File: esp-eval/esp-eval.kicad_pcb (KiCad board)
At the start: 2 copper layers, 26 parts, among them J1 ESP-ADAPT-1, J10 ESP-ADAPT-2-SHIELD, J2 ESP-ADAPT-2, J3 ESP-ADAPT-1-DBG, J4 ESP-ADAPT-2-DBG, J5 GPIO0-SEL, J6 GPIO2-SEL, J7 GPIO15-SEL, J8 USB-FTDI, J9 ESP-ADAPT-1-SHIELD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

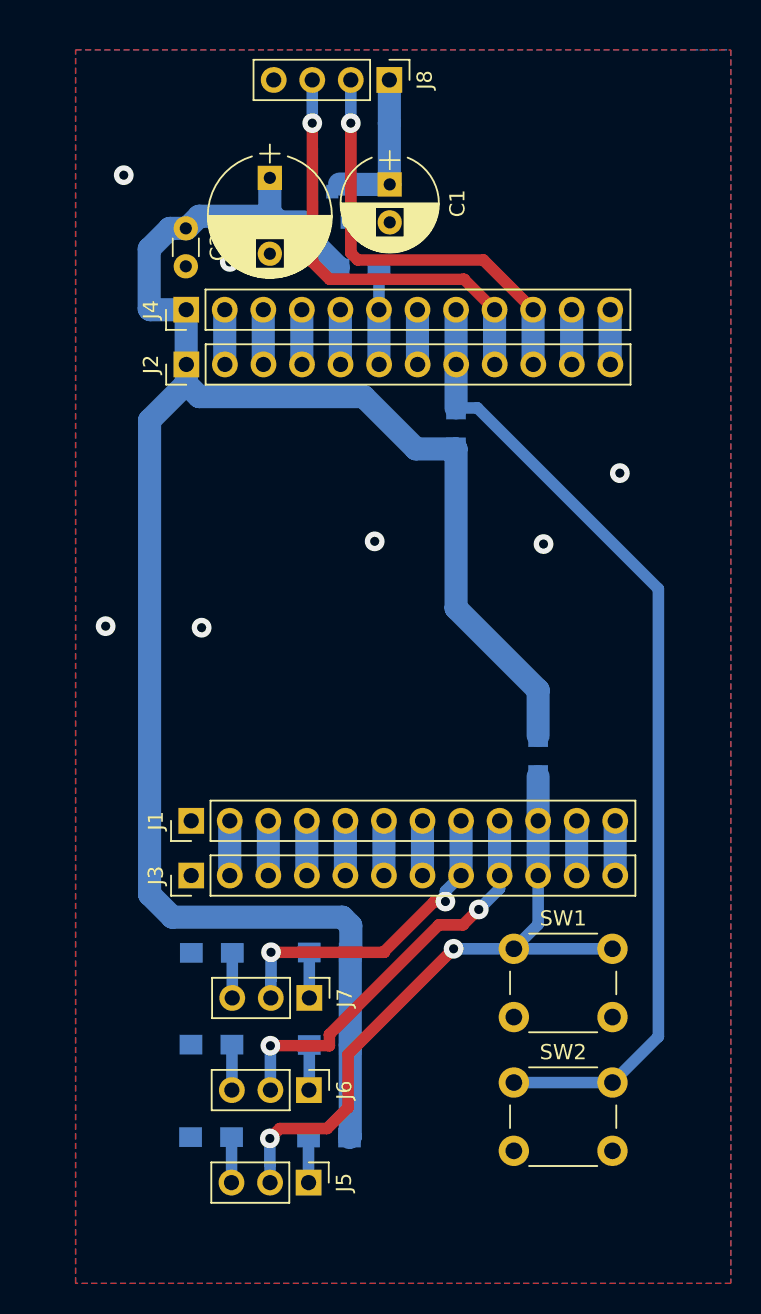
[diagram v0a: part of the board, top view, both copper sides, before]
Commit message: otwory montazowe
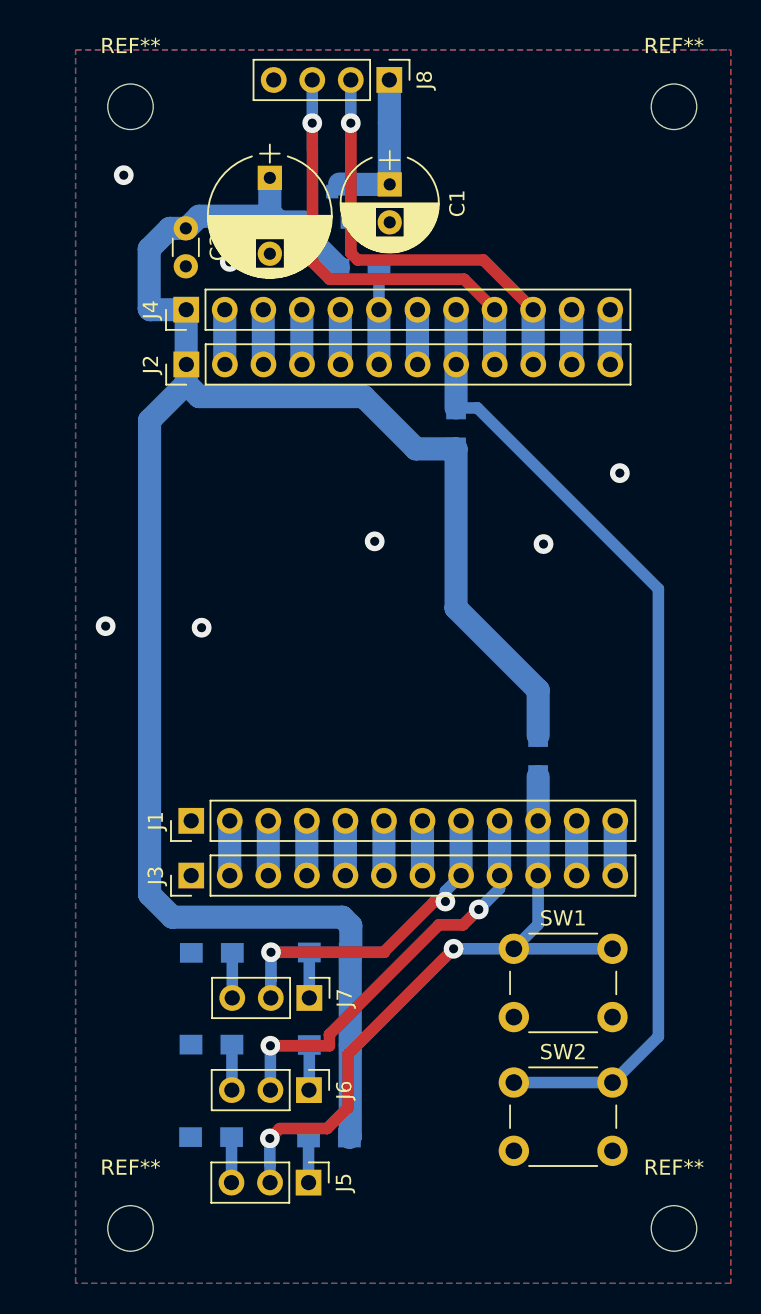
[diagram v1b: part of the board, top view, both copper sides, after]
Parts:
- added REF**: MountingHole_3mm, Mounting_Holes:MountingHole_3mm, F.Cu at (114.7, 23.5)
- added REF**: MountingHole_3mm, Mounting_Holes:MountingHole_3mm, F.Cu at (78.9, 23.5)
- added REF**: MountingHole_3mm, Mounting_Holes:MountingHole_3mm, F.Cu at (114.7, 97.4)
- added REF**: MountingHole_3mm, Mounting_Holes:MountingHole_3mm, F.Cu at (78.9, 97.4)
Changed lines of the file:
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@@
     (tracks 287)
     (zones 0)
-    (modules 26)
+    (modules 30)
     (nets 53)
   )
@@
     (add_net GND)
     (add_net VBUS)
+  )
+  (module Mounting_Holes:MountingHole_3mm (layer F.Cu)
+    (at 114.681 23.495)
+    (descr "Mounting Hole 3mm, no annular")
+    (tags "mounting hole 3mm no annular")
+    (attr virtual)
+    (fp_text reference REF** (at 0 -4) (layer F.SilkS)
+      (effects (font (size 1 1) (thickness 0.15)))
+    )
+    (fp_text value MountingHole_3mm (at 0 4) (layer F.Fab)
+      (effects (font (size 1 1) (thickness 0.15)))
+    )
+    (fp_circle (center 0 0) (end 3.25 0) (layer F.CrtYd) (width 0.05))
+    (fp_circle (center 0 0) (end 3 0) (layer Cmts.User) (width 0.15))
+    (fp_text user %R (at 0.3 0) (layer F.Fab)
+      (effects (font (size 1 1) (thickness 0.15)))
+    )
+    (pad 1 np_thru_hole circle (at 0 0) (size 3 3) (drill 3) (layers *.Cu *.Mask))
+  )
+  (module Mounting_Holes:MountingHole_3mm (layer F.Cu)
+    (at 78.867 23.495)
+    (descr "Mounting Hole 3mm, no annular")
+    (tags "mounting hole 3mm no annular")
+    (attr virtual)
+    (fp_text reference REF** (at 0 -4) (layer F.SilkS)
+      (effects (font (size 1 1) (thickness 0.15)))
+    )
+    (fp_text value MountingHole_3mm (at 0 4) (layer F.Fab)
+      (effects (font (size 1 1) (thickness 0.15)))
+    )
+    (fp_circle (center 0 0) (end 3.25 0) (layer F.CrtYd) (width 0.05))
+    (fp_circle (center 0 0) (end 3 0) (layer Cmts.User) (width 0.15))
+    (fp_text user %R (at 0.3 0) (layer F.Fab)
+      (effects (font (size 1 1) (thickness 0.15)))
+    )
+    (pad 1 np_thru_hole circle (at 0 0) (size 3 3) (drill 3) (layers *.Cu *.Mask))
+  )
+  (module Mounting_Holes:MountingHole_3mm (layer F.Cu)
+    (at 114.681 97.409)
+    (descr "Mounting Hole 3mm, no annular")
+    (tags "mounting hole 3mm no annular")
+    (attr virtual)
+    (fp_text reference REF** (at 0 -4) (layer F.SilkS)
+      (effects (font (size 1 1) (thickness 0.15)))
+    )
+    (fp_text value MountingHole_3mm (at 0 4) (layer F.Fab)
+      (effects (font (size 1 1) (thickness 0.15)))
+    )
+    (fp_circle (center 0 0) (end 3.25 0) (layer F.CrtYd) (width 0.05))
+    (fp_circle (center 0 0) (end 3 0) (layer Cmts.User) (width 0.15))
+    (fp_text user %R (at 0.3 0) (layer F.Fab)
+      (effects (font (size 1 1) (thickness 0.15)))
+    )
+    (pad 1 np_thru_hole circle (at 0 0) (size 3 3) (drill 3) (layers *.Cu *.Mask))
   )
   (module Capacitors_ThroughHole:C_Disc_D3.0mm_W1.6mm_P2.50mm (layer F.Cu)
@@
     )
   )
+  (module Mounting_Holes:MountingHole_3mm (layer F.Cu)
+    (at 78.867 97.409)
+    (descr "Mounting Hole 3mm, no annular")
+    (tags "mounting hole 3mm no annular")
+    (attr virtual)
+    (fp_text reference REF** (at 0 -4) (layer F.SilkS)
+      (effects (font (size 1 1) (thickness 0.15)))
+    )
+    (fp_text value MountingHole_3mm (at 0 4) (layer F.Fab)
+      (effects (font (size 1 1) (thickness 0.15)))
+    )
+    (fp_text user %R (at 0.3 0) (layer F.Fab)
+      (effects (font (size 1 1) (thickness 0.15)))
+    )
+    (fp_circle (center 0 0) (end 3 0) (layer Cmts.User) (width 0.15))
+    (fp_circle (center 0 0) (end 3.25 0) (layer F.CrtYd) (width 0.05))
+    (pad 1 np_thru_hole circle (at 0 0) (size 3 3) (drill 3) (layers *.Cu *.Mask))
+  )
   (via (at 106.0831 52.3113) (size 1.3) (drill 0.6) (layers F.Cu B.Cu) (net 1))

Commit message: ulozenie plytek
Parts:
- moved U2 19.3 mm to (53.6, 51.5)
- moved J9 19.3 mm to (25.6, 70.9)
- moved J10 19.3 mm to (25.3, 40.8)

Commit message: napisy
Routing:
- net /RXD0: track 28.9 -> 29.4 mm, vias 1 -> 2
- net /TXD0: track 28.6 -> 29.0 mm, vias 1 -> 2
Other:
- board text added: "0"
- board text added: "1"
- board text added: "5V"
- board text added: "GND"
- board text added: "GPIO0"
- board text added: "GPIO15"
- board text added: "GPIO2"
- board text added: "RST"
- board text added: "RXD0"
- board text added: "TXD0"
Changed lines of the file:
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@@
   (general
     (thickness 1.6)
-    (drawings 4)
-    (tracks 287)
+    (drawings 15)
+    (tracks 298)
     (zones 0)
     (modules 30)
@@
   (layers
     (0 F.Cu signal)
-    (31 B.Cu signal)
+    (31 B.Cu signal hide)
     (32 B.Adhes user)
     (33 F.Adhes user hide)
@@
     (pad 1 np_thru_hole circle (at 0 0) (size 3 3) (drill 3) (layers *.Cu *.Mask))
   )
+  (gr_text RST (at 116.84 89.9922 90) (layer F.Cu)
+    (effects (font (size 1.5 1.5) (thickness 0.3)))
+  )
+  (gr_text GPIO0 (at 116.7892 81.3308 90) (layer F.Cu)
+    (effects (font (size 1.5 1.5) (thickness 0.3)))
+  )
+  (gr_text 1 (at 90.5764 96.7232) (layer F.Cu)
+    (effects (font (size 1.5 1.5) (thickness 0.3)))
+  )
+  (gr_text 0 (at 85.4964 96.774) (layer F.Cu)
+    (effects (font (size 1.5 1.5) (thickness 0.3)))
+  )
+  (gr_text GPIO0 (at 82.8548 91.3384) (layer F.Cu)
+    (effects (font (size 1.5 1.5) (thickness 0.3)))
+  )
+  (gr_text GPIO2 (at 82.8802 85.2932) (layer F.Cu)
+    (effects (font (size 1.5 1.5) (thickness 0.3)))
+  )
+  (gr_text GPIO15 (at 82.2198 79.0956) (layer F.Cu)
+    (effects (font (size 1.5 1.5) (thickness 0.3)))
+  )
+  (gr_text 5V (at 107.5436 21.9964 90) (layer F.Cu)
+    (effects (font (size 1.5 1.5) (thickness 0.3)))
+  )
+  (gr_text TXD0 (at 105.0036 23.1648 90) (layer F.Cu)
+    (effects (font (size 1.5 1.5) (thickness 0.3)))
+  )
+  (gr_text RXD0 (at 102.4636 23.2918 90) (layer F.Cu)
+    (effects (font (size 1.5 1.5) (thickness 0.3)))
+  )
+  (gr_text GND (at 99.8982 22.6314 90) (layer F.Cu)
+    (effects (font (size 1.5 1.5) (thickness 0.3)))
+  )
   (dimension 81.127636 (width 0.3) (layer F.SilkS)
     (gr_text "81,128 mm" (at 126.825905 60.383783 89.94618432) (layer F.SilkS)
@@
   (via (at 90.8431 24.5745) (size 1.3) (drill 0.6) (layers F.Cu B.Cu) (net 17))
   (segment (start 90.8431 24.5745) (end 90.8431 21.7297) (width 0.762) (layer B.Cu) (net 17) (status 20))
-  (segment (start 100.8505 34.8615) (end 102.8575 36.8685) (width 0.762) (layer F.Cu) (net 17) (status 20))
-  (segment (start 91.9861 34.8615) (end 100.8505 34.8615) (width 0.762) (layer F.Cu) (net 17))
-  (segment (start 90.8685 33.7439) (end 91.9861 34.8615) (width 0.762) (layer F.Cu) (net 17))
-  (segment (start 90.8431 24.5745) (end 90.8685 33.7439) (width 0.762) (layer F.Cu) (net 17))
+  (segment (start 90.8431 24.5745) (end 90.8558 32.9692) (width 0.762) (layer F.Cu) (net 17))
+  (segment (start 90.8558 32.9692) (end 90.8558 33.02) (width 0.762) (layer F.Cu) (net 17))
+  (via (at 101.3714 34.3916) (size 1.3) (drill 0.6) (layers F.Cu B.Cu) (net 17))
+  (segment (start 90.8558 33.02) (end 92.2274 34.3916) (width 0.762) (layer F.Cu) (net 17))
+  (segment (start 92.2274 34.3916) (end 101.3714 34.3916) (width 0.762) (layer F.Cu) (net 17))
+  (segment (start 101.3714 34.3916) (end 101.9302 34.3916) (width 0.762) (layer B.Cu) (net 17))
+  (segment (start 102.8575 35.3189) (end 102.8575 36.8685) (width 0.762) (layer B.Cu) (net 17))
+  (segment (start 101.9302 34.3916) (end 102.8575 35.3189) (width 0.762) (layer B.Cu) (net 17))
   (segment (start 105.3975 40.464898) (end 105.407502 40.4749) (width 1.524) (layer B.Cu) (net 18) (status 30))
   (segment (start 105.3975 36.8685) (end 105.3975 40.464898) (width 1.524) (layer B.Cu) (net 18) (status 30))
   (via (at 93.3831 24.5745) (size 1.3) (drill 0.6) (layers F.Cu B.Cu) (net 18))
   (segment (start 93.3831 24.5745) (end 93.3831 21.7297) (width 0.762) (layer B.Cu) (net 18) (status 20))
-  (segment (start 102.12049 33.59149) (end 105.3975 36.8685) (width 0.762) (layer F.Cu) (net 18) (status 20))
-  (segment (start 93.84029 33.59149) (end 102.12049 33.59149) (width 0.762) (layer F.Cu) (net 18))
-  (segment (start 93.3831 33.1343) (end 93.84029 33.59149) (width 0.762) (layer F.Cu) (net 18))
-  (segment (start 93.3831 24.5745) (end 93.3831 33.1343) (width 0.762) (layer F.Cu) (net 18))
+  (segment (start 93.3831 24.5745) (end 93.3958 32.7406) (width 0.762) (layer F.Cu) (net 18))
+  (via (at 103.978436 34.264374) (size 1.3) (drill 0.6) (layers F.Cu B.Cu) (net 18))
+  (segment (start 102.516163 32.802101) (end 103.978436 34.264374) (width 0.762) (layer F.Cu) (net 18))
+  (segment (start 93.3958 32.7406) (end 93.457301 32.802101) (width 0.762) (layer F.Cu) (net 18))
+  (segment (start 93.457301 32.802101) (end 102.516163 32.802101) (width 0.762) (layer F.Cu) (net 18))
+  (segment (start 104.12751 34.413448) (end 104.12751 34.42991) (width 0.762) (layer B.Cu) (net 18))
+  (segment (start 103.978436 34.264374) (end 104.12751 34.413448) (width 0.762) (layer B.Cu) (net 18))
+  (segment (start 104.12751 34.42991) (end 104.8766 35.179) (width 0.762) (layer B.Cu) (net 18))
+  (segment (start 105.3975 35.666419) (end 105.3975 36.8685) (width 0.762) (layer B.Cu) (net 18))
+  (segment (start 104.910081 35.179) (end 105.3975 35.666419) (width 0.762) (layer B.Cu) (net 18))
+  (segment (start 104.8766 35.179) (end 104.910081 35.179) (width 0.762) (layer B.Cu) (net 18))
   (segment (start 100.3175 40.464898) (end 100.327502 40.4749) (width 1.524) (layer B.Cu) (net 19) (status 30))
   (segment (start 100.3175 36.8685) (end 100.3175 40.464898) (width 1.524) (layer B.Cu) (net 19) (status 30))

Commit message: fixes;
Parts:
- removed the REF** at (114.7, 23.5)
- removed the REF** at (78.9, 23.5)
- removed the REF** at (114.7, 97.4)
- added C1: 47u, Capacitors_ThroughHole:CP_Radial_D6.3mm_P2.50mm, B.Cu at (142.9, 132.4)
- added C2: 220u, Capacitors_ThroughHole:CP_Radial_D8.0mm_P5.00mm, B.Cu at (142.5, 124.5)
- added C3: 100n, Capacitors_ThroughHole:C_Disc_D3.0mm_W1.6mm_P2.50mm, B.Cu at (145.8, 119.0)
- added J1: ESP-ADAPT-1, Pin_Headers:Pin_Header_Straight_1x12_Pitch2.54mm, B.Cu at (184.8, 119.3)
- added J10: ESP-ADAPT-2-SHIELD, Pin_Headers:Pin_Header_Straight_1x12_Pitch2.54mm, B.Cu at (68.3, 142.7)
- added J2: ESP-ADAPT-2, Pin_Headers:Pin_Header_Straight_1x12_Pitch2.54mm, B.Cu at (154.8, 119.0)
- added J3: ESP-ADAPT-1-DBG, Pin_Headers:Pin_Header_Straight_1x12_Pitch2.54mm, B.Cu at (188.5, 119.3)
- added J4: ESP-ADAPT-2-DBG, Pin_Headers:Pin_Header_Straight_1x12_Pitch2.54mm, B.Cu at (151.2, 119.0)
- added J5: GPIO0-SEL, Pin_Headers:Pin_Header_Straight_1x03_Pitch2.54mm, B.Cu at (208.7, 127.1)
- added J6: GPIO2-SEL, Pin_Headers:Pin_Header_Straight_1x03_Pitch2.54mm, B.Cu at (202.6, 127.1)
- added J7: GPIO15-SEL, Pin_Headers:Pin_Header_Straight_1x03_Pitch2.54mm, B.Cu at (196.5, 127.1)
- added J8: USB-FTDI, Pin_Headers:Pin_Header_Straight_1x04_Pitch2.54mm, B.Cu at (136.0, 132.4)
- added J9: ESP-ADAPT-1-SHIELD, Pin_Headers:Pin_Header_Straight_1x12_Pitch2.54mm, B.Cu at (68.6, 112.6)
- added R1: 10k, Resistors_SMD:R_0805_HandSoldering, F.Cu at (180.6, 142.2)
- added R2: 10k, Resistors_SMD:R_0805_HandSoldering, F.Cu at (159.0, 136.8)
- added R3: 10k, Resistors_SMD:R_0805_HandSoldering, F.Cu at (205.7, 128.4)
- added R4: 10k, Resistors_SMD:R_0805_HandSoldering, F.Cu at (205.7, 120.6)
- added R5: 10k, Resistors_SMD:R_0805_HandSoldering, F.Cu at (148.4, 130.3)
- added R6: 10k, Resistors_SMD:R_0805_HandSoldering, F.Cu at (199.6, 128.5)
- added R7: 10k, Resistors_SMD:R_0805_HandSoldering, F.Cu at (199.6, 120.7)
- added R8: 10k, Resistors_SMD:R_0805_HandSoldering, F.Cu at (193.5, 128.5)
- added R9: 10k, Resistors_SMD:R_0805_HandSoldering, F.Cu at (193.5, 120.7)
- added REF**: MountingHole_3mm, Mounting_Holes:MountingHole_3mm, B.Cu at (211.7, 115.3)
- added REF**: MountingHole_3mm, Mounting_Holes:MountingHole_3mm, B.Cu at (211.7, 151.1)
- added REF**: MountingHole_3mm, Mounting_Holes:MountingHole_3mm, B.Cu at (137.8, 115.3)
- added REF**: MountingHole_3mm, Mounting_Holes:MountingHole_3mm, B.Cu at (137.8, 151.1)
- added REF**: MountingHole_3mm, Mounting_Holes:MountingHole_3mm, F.Cu at (137.8, 53.0)
- added REF**: MountingHole_3mm, Mounting_Holes:MountingHole_3mm, F.Cu at (137.8, 88.8)
- added REF**: MountingHole_3mm, Mounting_Holes:MountingHole_3mm, F.Cu at (211.7, 53.0)
- added SW1: SW-GPIO0, Buttons_Switches_ThroughHole:SW_PUSH_6mm, B.Cu at (193.3, 140.6)
- added SW2: SW-RST, Buttons_Switches_ThroughHole:SW_PUSH_6mm, B.Cu at (202.1, 140.6)
- added U1: MCP1700-3302E_SOT23, TO_SOT_Packages_SMD:SOT-23, F.Cu at (144.4, 128.6)
- added U2: ESP-12E, ESP8266:ESP-12E_SMD, B.Cu at (96.7, 132.0)
- moved REF** 133.1 mm to (211.7, 88.8), turned to 90 degrees
- moved R4 121.8 mm to (205.7, 83.5), turned to 270 degrees
- moved J5 119.4 mm to (208.7, 77.0), turned to 0 degrees
- moved R7 115.4 mm to (199.6, 83.4), turned to 270 degrees
- moved R3 114.9 mm to (205.7, 75.7), turned to 270 degrees
- moved J6 112.5 mm to (202.6, 77.0), turned to 0 degrees
- moved R9 109.4 mm to (193.6, 83.4), turned to 270 degrees
- moved R6 108.1 mm to (199.6, 75.6), turned to 270 degrees
- moved J3 106.1 mm to (188.5, 84.8), turned to 180 degrees
- moved J7 106.0 mm to (196.5, 77.0), turned to 0 degrees
- moved J1 103.0 mm to (184.8, 84.8), turned to 180 degrees
- moved R8 101.6 mm to (193.5, 75.6), turned to 270 degrees
- moved SW2 100.9 mm to (202.1, 63.5), turned to 90 degrees
- moved SW1 90.5 mm to (193.3, 63.5), turned to 90 degrees
- moved J2 84.9 mm to (154.8, 85.1), turned to 180 degrees
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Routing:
- net (no net): track 0.00 -> 793.6 mm, vias 0 -> 31
- added copper zone on B.Cu, net (none)
- added copper zone on F.Cu, net (none)
